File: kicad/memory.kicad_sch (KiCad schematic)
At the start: 8 parts, among them U6 Address_Decoder, U7 W65C22S, U8 AT28C256, U9 AS6C4008

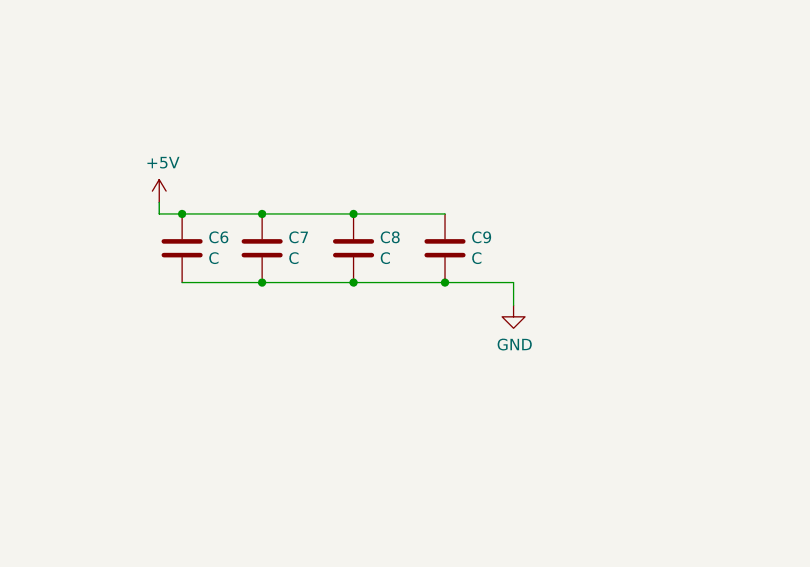
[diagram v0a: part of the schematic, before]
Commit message: update computer, move test program to use native mode
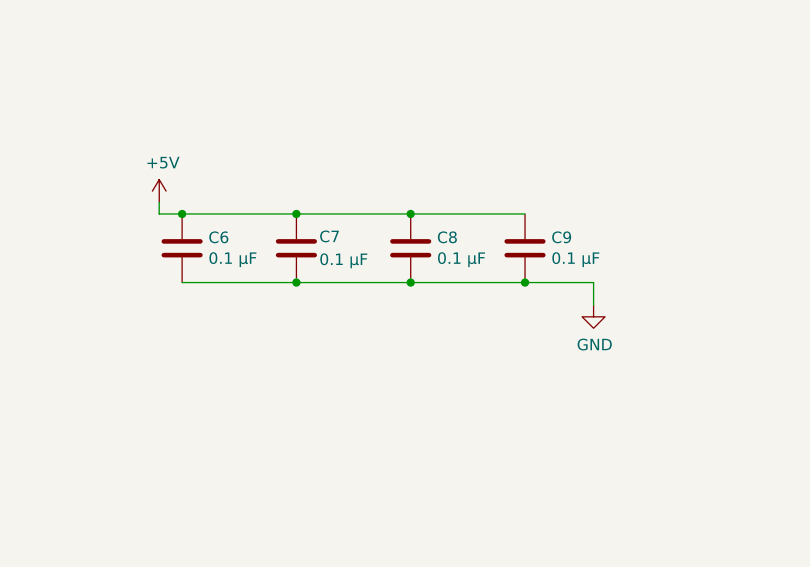
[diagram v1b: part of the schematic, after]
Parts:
- C6, C7, C8, C9: value C -> 0.1 µF
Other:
- moved on the sheet: C7, C8, C9
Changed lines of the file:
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@@
 (kicad_sch (version 20211123) (generator eeschema)
   (paper "A4")
-  (junction (at 154.94 146.05) (diameter 0) (color 0 0 0 0)
-  )
-  (junction (at 165.1 146.05) (diameter 0) (color 0 0 0 0)
-  )
-  (junction (at 165.1 138.43) (diameter 0) (color 0 0 0 0)
-  )
-  (junction (at 175.26 146.05) (diameter 0) (color 0 0 0 0)
-  )
-  (junction (at 154.94 138.43) (diameter 0) (color 0 0 0 0)
+  (junction (at 171.45 146.05) (diameter 0) (color 0 0 0 0)
+  )
+  (junction (at 171.45 138.43) (diameter 0) (color 0 0 0 0)
+  )
+  (junction (at 158.75 146.05) (diameter 0) (color 0 0 0 0)
+  )
+  (junction (at 184.15 146.05) (diameter 0) (color 0 0 0 0)
   )
   (junction (at 146.05 138.43) (diameter 0) (color 0 0 0 0)
+  )
+  (junction (at 158.75 138.43) (diameter 0) (color 0 0 0 0)
   )
   (junction (at 118.11 74.93) (diameter 0) (color 0 0 0 0)
@@
     (stroke (width 0) (type default) (color 0 0 0 0))
   )
-  (wire (pts (xy 175.26 138.43) (xy 165.1 138.43))
-    (stroke (width 0) (type default) (color 0 0 0 0))
-  )
   (wire (pts (xy 44.45 45.72) (xy 35.56 45.72))
     (stroke (width 0) (type default) (color 0 0 0 0))
@@
     (stroke (width 0) (type default) (color 0 0 0 0))
   )
-  (wire (pts (xy 182.88 146.05) (xy 182.88 148.59))
+  (wire (pts (xy 191.77 146.05) (xy 191.77 148.59))
     (stroke (width 0) (type default) (color 0 0 0 0))
   )
@@
     (stroke (width 0) (type default) (color 0 0 0 0))
   )
-  (wire (pts (xy 165.1 146.05) (xy 175.26 146.05))
-    (stroke (width 0) (type default) (color 0 0 0 0))
-  )
   (bus (pts (xy 148.59 43.18) (xy 148.59 45.72))
     (stroke (width 0) (type default) (color 0 0 0 0))
@@
     (stroke (width 0) (type default) (color 0 0 0 0))
   )
+  (wire (pts (xy 158.75 138.43) (xy 171.45 138.43))
+    (stroke (width 0) (type default) (color 0 0 0 0))
+  )
   (wire (pts (xy 209.55 43.18) (xy 214.63 43.18))
     (stroke (width 0) (type default) (color 0 0 0 0))
   )
+  (wire (pts (xy 146.05 138.43) (xy 158.75 138.43))
+    (stroke (width 0) (type default) (color 0 0 0 0))
+  )
   (bus (pts (xy 180.34 76.2) (xy 180.34 78.74))
     (stroke (width 0) (type default) (color 0 0 0 0))
@@
     (stroke (width 0) (type default) (color 0 0 0 0))
   )
-  (wire (pts (xy 154.94 146.05) (xy 165.1 146.05))
+  (wire (pts (xy 146.05 146.05) (xy 158.75 146.05))
     (stroke (width 0) (type default) (color 0 0 0 0))
   )
@@
     (stroke (width 0) (type default) (color 0 0 0 0))
   )
-  (wire (pts (xy 154.94 138.43) (xy 146.05 138.43))
-    (stroke (width 0) (type default) (color 0 0 0 0))
-  )
   (wire (pts (xy 35.56 60.96) (xy 44.45 60.96))
     (stroke (width 0) (type default) (color 0 0 0 0))
@@
     (stroke (width 0) (type default) (color 0 0 0 0))
   )
-  (wire (pts (xy 175.26 146.05) (xy 182.88 146.05))
+  (wire (pts (xy 184.15 146.05) (xy 191.77 146.05))
     (stroke (width 0) (type default) (color 0 0 0 0))
   )
@@
     (stroke (width 0) (type default) (color 0 0 0 0))
   )
-  (wire (pts (xy 165.1 138.43) (xy 154.94 138.43))
+  (wire (pts (xy 171.45 138.43) (xy 184.15 138.43))
     (stroke (width 0) (type default) (color 0 0 0 0))
   )
@@
     (stroke (width 0) (type default) (color 0 0 0 0))
   )
+  (wire (pts (xy 171.45 146.05) (xy 184.15 146.05))
+    (stroke (width 0) (type default) (color 0 0 0 0))
+  )
   (wire (pts (xy 182.88 45.72) (xy 189.23 45.72))
     (stroke (width 0) (type default) (color 0 0 0 0))
@@
     (stroke (width 0) (type default) (color 0 0 0 0))
   )
+  (wire (pts (xy 158.75 146.05) (xy 171.45 146.05))
+    (stroke (width 0) (type default) (color 0 0 0 0))
+  )
   (wire (pts (xy 140.97 40.64) (xy 146.05 40.64))
     (stroke (width 0) (type default) (color 0 0 0 0))
@@
   )
   (wire (pts (xy 35.56 38.1) (xy 44.45 38.1))
-    (stroke (width 0) (type default) (color 0 0 0 0))
-  )
-  (wire (pts (xy 146.05 146.05) (xy 154.94 146.05))
     (stroke (width 0) (type default) (color 0 0 0 0))
   )
@@
       (effects (font (size 1.27 1.27)) (justify left))
     )
-    (property "Value" "C" (id 1) (at 148.971 143.383 0)
+    (property "Value" "0.1 µF" (id 1) (at 148.971 143.383 0)
       (effects (font (size 1.27 1.27)) (justify left))
     )
@@
     (pin "2")
   )
-  (symbol (lib_id "Device:C") (at 154.94 142.24 0) (unit 1)
-    (in_bom yes) (on_board yes)
-    (property "Reference" "C7" (id 0) (at 157.861 141.0716 0)
+  (symbol (lib_id "Device:C") (at 158.75 142.24 0) (unit 1)
+    (in_bom yes) (on_board yes)
+    (property "Reference" "C7" (id 0) (at 161.29 140.97 0)
       (effects (font (size 1.27 1.27)) (justify left))
     )
-    (property "Value" "C" (id 1) (at 157.861 143.383 0)
+    (property "Value" "0.1 µF" (id 1) (at 161.29 143.51 0)
       (effects (font (size 1.27 1.27)) (justify left))
     )
-    (property "Footprint" "" (id 2) (at 155.9052 146.05 0)
-      (effects (font (size 1.27 1.27)) hide)
-    )
-    (property "Datasheet" "~" (id 3) (at 154.94 142.24 0)
+    (property "Footprint" "" (id 2) (at 159.7152 146.05 0)
+      (effects (font (size 1.27 1.27)) hide)
+    )
+    (property "Datasheet" "~" (id 3) (at 158.75 142.24 0)
       (effects (font (size 1.27 1.27)) hide)
     )
@@
     (pin "2")
   )
-  (symbol (lib_id "Device:C") (at 165.1 142.24 0) (unit 1)
-    (in_bom yes) (on_board yes)
-    (property "Reference" "C8" (id 0) (at 168.021 141.0716 0)
+  (symbol (lib_id "Device:C") (at 171.45 142.24 0) (unit 1)
+    (in_bom yes) (on_board yes)
+    (property "Reference" "C8" (id 0) (at 174.371 141.0716 0)
       (effects (font (size 1.27 1.27)) (justify left))
     )
-    (property "Value" "C" (id 1) (at 168.021 143.383 0)
+    (property "Value" "0.1 µF" (id 1) (at 174.371 143.383 0)
       (effects (font (size 1.27 1.27)) (justify left))
     )
-    (property "Footprint" "" (id 2) (at 166.0652 146.05 0)
-      (effects (font (size 1.27 1.27)) hide)
-    )
-    (property "Datasheet" "~" (id 3) (at 165.1 142.24 0)
+    (property "Footprint" "" (id 2) (at 172.4152 146.05 0)
+      (effects (font (size 1.27 1.27)) hide)
+    )
+    (property "Datasheet" "~" (id 3) (at 171.45 142.24 0)
       (effects (font (size 1.27 1.27)) hide)
     )
@@
     (pin "2")
   )
-  (symbol (lib_id "Device:C") (at 175.26 142.24 0) (unit 1)
-    (in_bom yes) (on_board yes)
-    (property "Reference" "C9" (id 0) (at 178.181 141.0716 0)
+  (symbol (lib_id "Device:C") (at 184.15 142.24 0) (unit 1)
+    (in_bom yes) (on_board yes)
+    (property "Reference" "C9" (id 0) (at 187.071 141.0716 0)
       (effects (font (size 1.27 1.27)) (justify left))
     )
-    (property "Value" "C" (id 1) (at 178.181 143.383 0)
+    (property "Value" "0.1 µF" (id 1) (at 187.071 143.383 0)
       (effects (font (size 1.27 1.27)) (justify left))
     )
-    (property "Footprint" "" (id 2) (at 176.2252 146.05 0)
-      (effects (font (size 1.27 1.27)) hide)
-    )
-    (property "Datasheet" "~" (id 3) (at 175.26 142.24 0)
+    (property "Footprint" "" (id 2) (at 185.1152 146.05 0)
+      (effects (font (size 1.27 1.27)) hide)
+    )
+    (property "Datasheet" "~" (id 3) (at 184.15 142.24 0)
       (effects (font (size 1.27 1.27)) hide)
     )
@@
     (pin "1")
   )
-  (symbol (lib_id "power:GND") (at 182.88 148.59 0) (unit 1)
-    (in_bom yes) (on_board yes)
-    (property "Reference" "#PWR030" (id 0) (at 182.88 154.94 0)
-      (effects (font (size 1.27 1.27)) hide)
-    )
-    (property "Value" "GND" (id 1) (at 183.007 152.9842 0))
-    (property "Footprint" "" (id 2) (at 182.88 148.59 0)
-      (effects (font (size 1.27 1.27)) hide)
-    )
-    (property "Datasheet" "" (id 3) (at 182.88 148.59 0)
-      (effects (font (size 1.27 1.27)) hide)
-    )
+  (symbol (lib_id "power:GND") (at 191.77 148.59 0) (unit 1)
+    (in_bom yes) (on_board yes)
+    (property "Reference" "#PWR030" (id 0) (at 191.77 154.94 0)
+      (effects (font (size 1.27 1.27)) hide)
+    )
+    (property "Value" "GND" (id 1) (at 191.897 152.9842 0))
+    (property "Footprint" "" (id 2) (at 191.77 148.59 0)
+      (effects (font (size 1.27 1.27)) hide)
+    )
+    (property "Datasheet" "" (id 3) (at 191.77 148.59 0)
+      (effects (font (size 1.27 1.27)) hide)
+    )

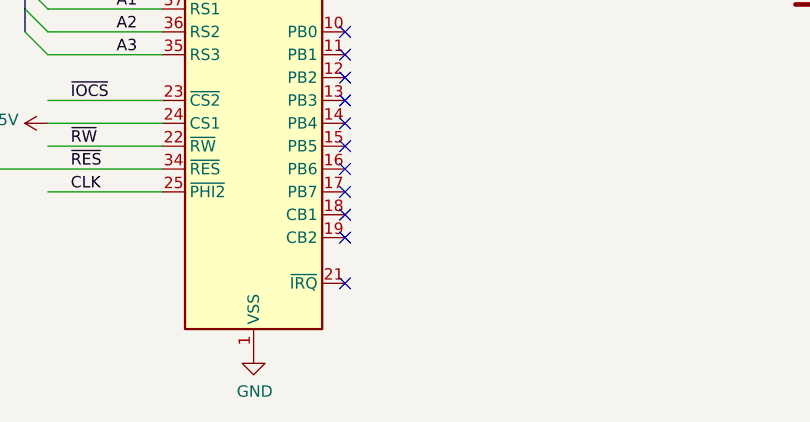
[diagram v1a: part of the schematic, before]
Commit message: connect IRQ output of 65C22 to CPU NMI
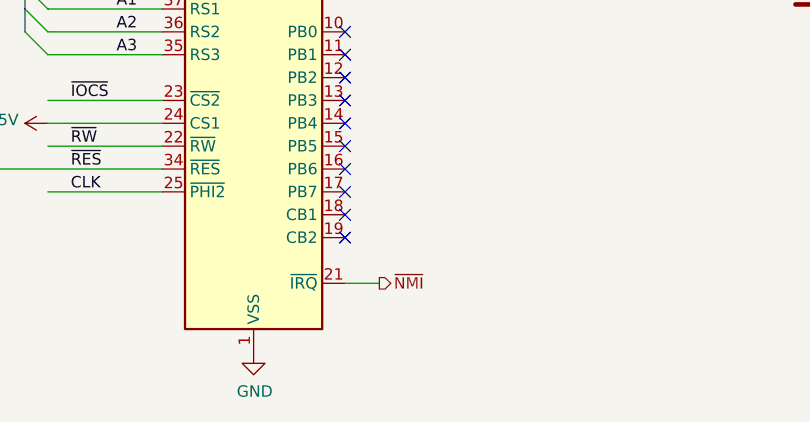
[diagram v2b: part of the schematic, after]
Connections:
- net ~{NMI}: now reaches U7.21 (~{IRQ})
- no-connect marks 24 -> 23
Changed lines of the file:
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@@
   (no_connect (at 93.98 123.19))
   (no_connect (at 93.98 133.35))
-  (no_connect (at 93.98 173.99))
   (no_connect (at 93.98 156.21))
   (no_connect (at 93.98 125.73))
@@
     (stroke (width 0) (type default) (color 0 0 0 0))
   )
+  (wire (pts (xy 93.98 173.99) (xy 97.79 173.99))
+    (stroke (width 0) (type default) (color 0 0 0 0))
+  )
   (wire (pts (xy 35.56 60.96) (xy 44.45 60.96))
     (stroke (width 0) (type default) (color 0 0 0 0))
@@
     (effects (font (size 1.27 1.27)) (justify right))
   )
+  (hierarchical_label "~{NMI}" (shape output) (at 97.79 173.99 0)
+    (effects (font (size 1.27 1.27)) (justify left))
+  )
   (symbol (lib_id "power:+5V") (at 199.39 33.02 270) (unit 1)

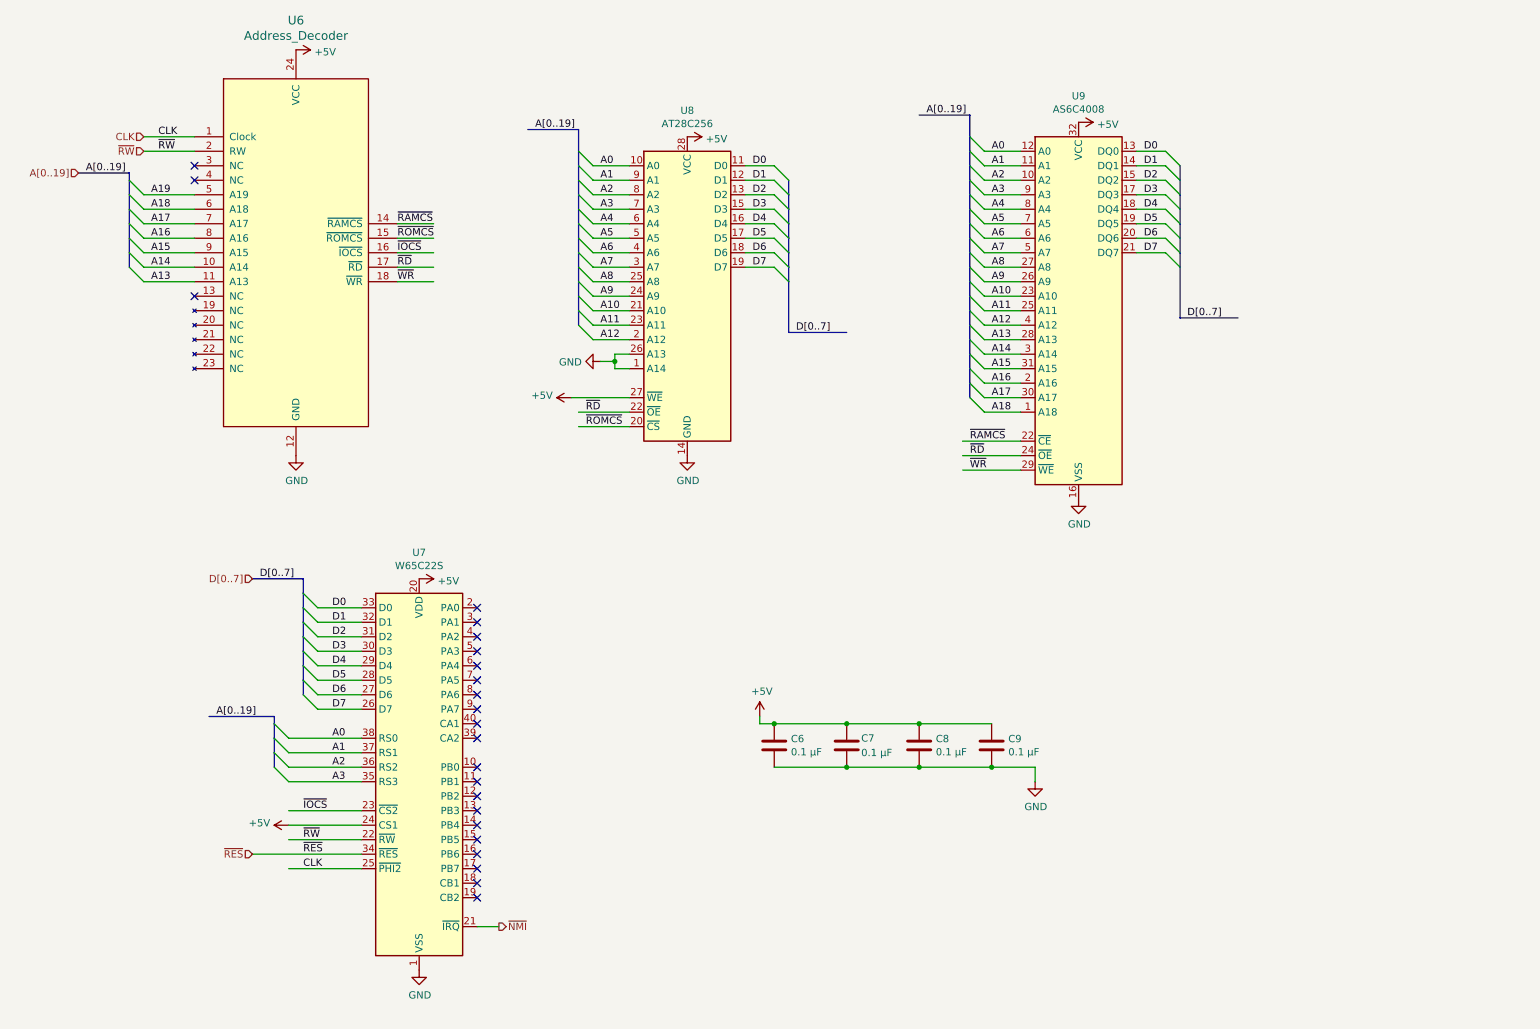
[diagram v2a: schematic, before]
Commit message: add extra 512 kB RAM, 74AC138 for future use
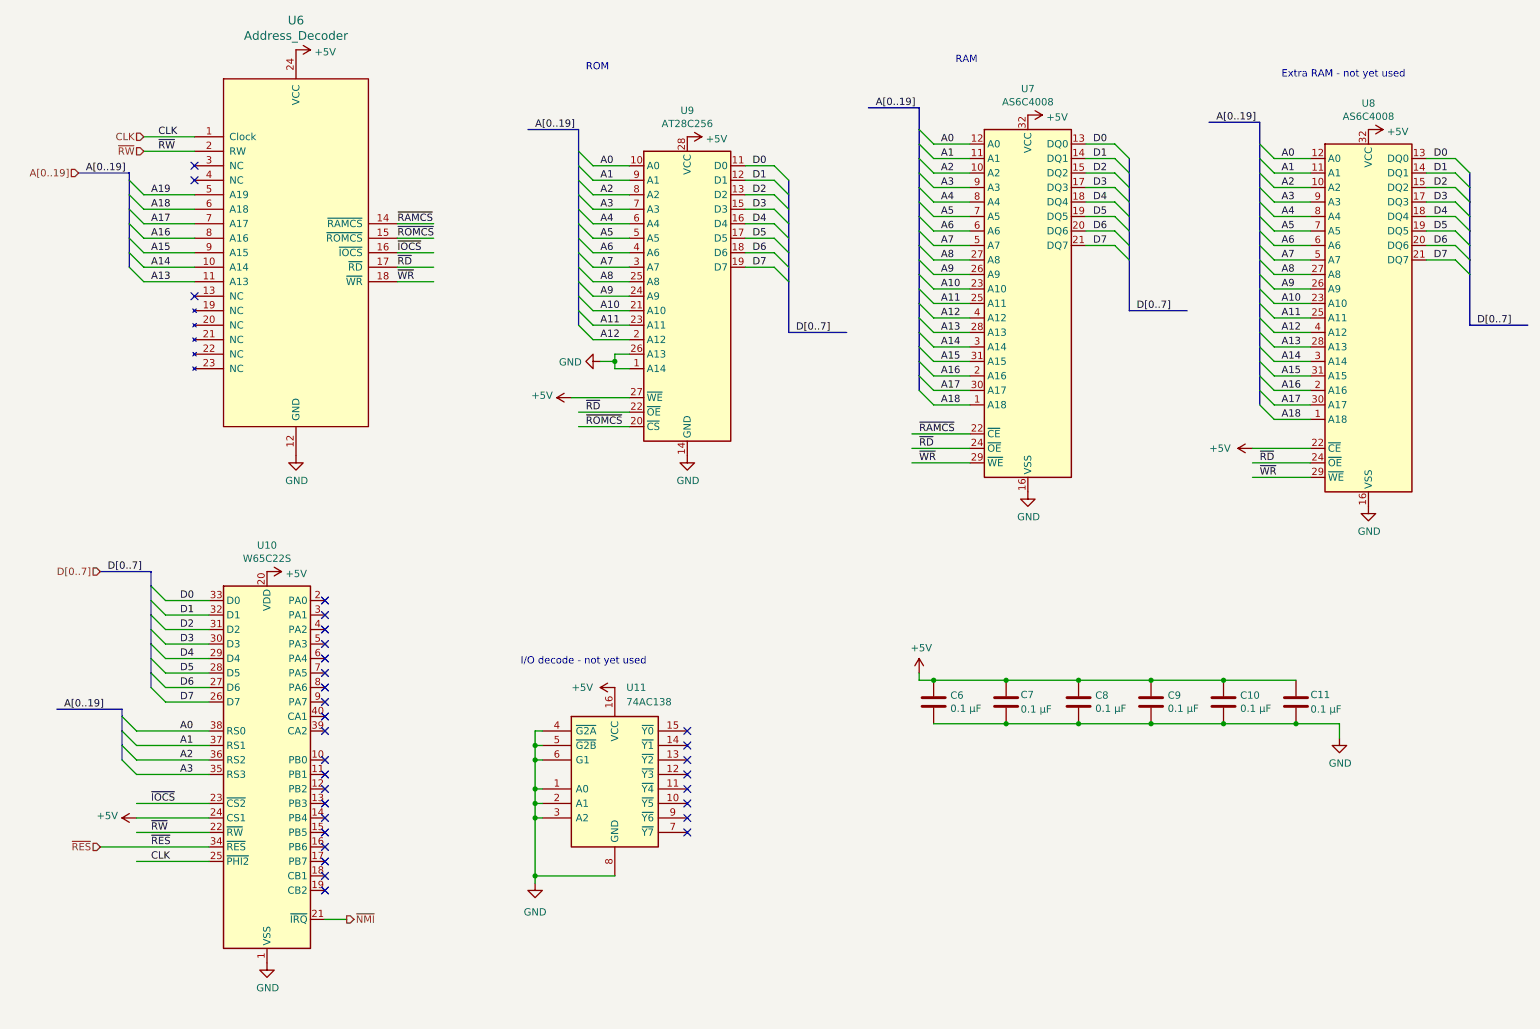
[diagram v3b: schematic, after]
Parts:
- added C10, C11: 0.1 µF, symbol Device:C
- added U11: 74AC138, symbol project:74AC138
- added U8: AS6C4008, symbol project:AS6C4008
- renumbered U7 to U10, U9 to U7, U8 to U9
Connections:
- net +5V: now also C10.1, C11.1, U11.16 (VCC), U8.22 (~{CE}), U8.32 (VCC)
- net A0: now also U8.12 (A0)
- net A1: now also U8.11 (A1)
- net A10: now also U8.23 (A10)
- net A11: now also U8.25 (A11)
- net A12: now also U8.4 (A12)
- net A13: now also U8.28 (A13)
- net A14: now also U8.3 (A14)
- net A15: now also U8.31 (A15)
- net A16: now also U8.2 (A16)
- net A17: now also U8.30 (A17)
- net A18: now also U8.1 (A18)
- net A2: now also U8.10 (A2)
- net A3: now also U8.9 (A3)
- net A4: now also U8.8 (A4)
- net A5: now also U8.7 (A5)
- net A6: now also U8.6 (A6)
- net A7: now also U8.5 (A7)
- net A8: now also U8.27 (A8)
- net A9: now also U8.26 (A9)
- net D0: now also U8.13 (DQ0)
- net D1: now also U8.14 (DQ1)
- net D2: now also U8.15 (DQ2)
- net D3: now also U8.17 (DQ3)
- net D4: now also U8.18 (DQ4)
- net D5: now also U8.19 (DQ5)
- net D6: now also U8.20 (DQ6)
- net D7: now also U8.21 (DQ7)
- net GND: now also C10.2, C11.2, U11.1 (A0), U11.2 (A1), U11.3 (A2), U11.4 (~{G2A}), U11.5 (~{G2B}), U11.6 (G1), U11.8 (GND), U8.16 (VSS)
- net ~{RD}: now also U8.24 (~{OE})
- net ~{WR}: now also U8.29 (~{WE})
- no-connect marks 23 -> 31
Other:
- note added: "Extra RAM - not yet used"
- note added: "I/O decode - not yet used"
- note added: "RAM"
- note added: "ROM"
- moved on the sheet: C6, C7, C8, C9, U10, U7
